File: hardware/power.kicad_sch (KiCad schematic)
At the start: 16 parts, among them J6 USB_C_Receptacle, Q1 DMG2307L, Q2 DMG2307L, Q3 BSD235N, U5 AP9101CK, U6 MIC5504-3.3YM5

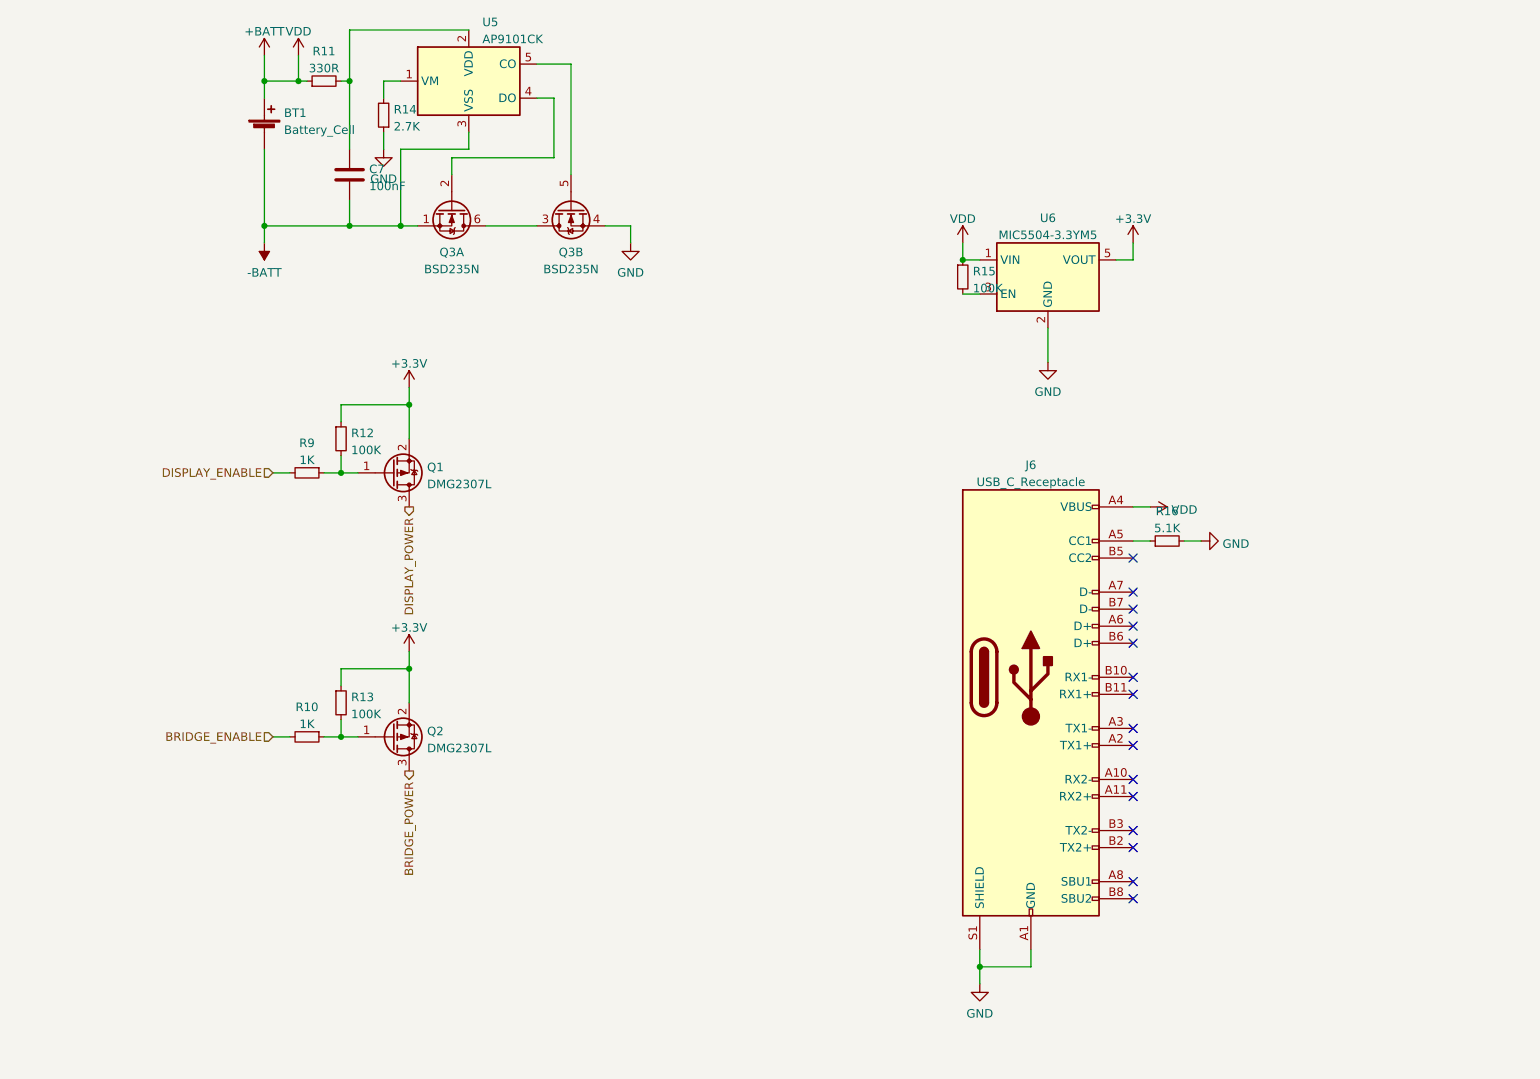
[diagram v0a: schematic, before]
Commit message: Updated schematic according to reference design
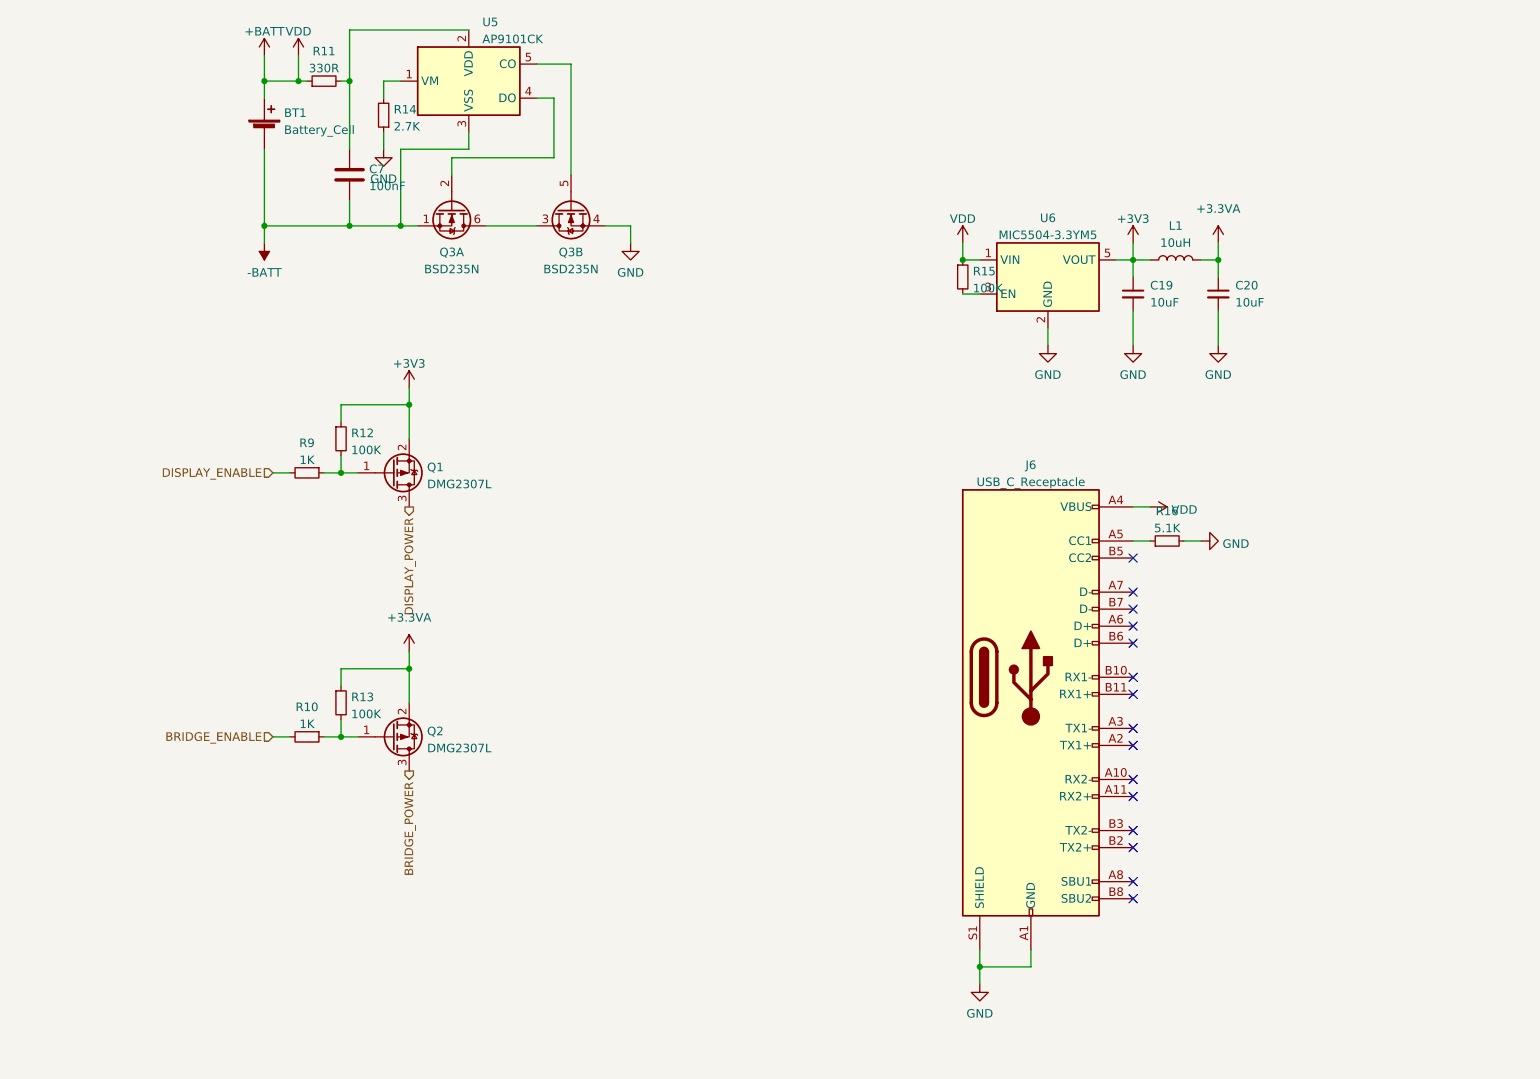
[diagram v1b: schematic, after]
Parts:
- added C19, C20: 10uF, symbol Device:C_Small
- added L1: 10uH, symbol Device:L
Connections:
- net +3V3: now also C19.1, L1.1; no longer Q2.2 (S), R13.1
- net GND: now also C19.2, C20.2
- new net +3.3VA: C20.1, L1.2, Q2.2 (S), R13.1

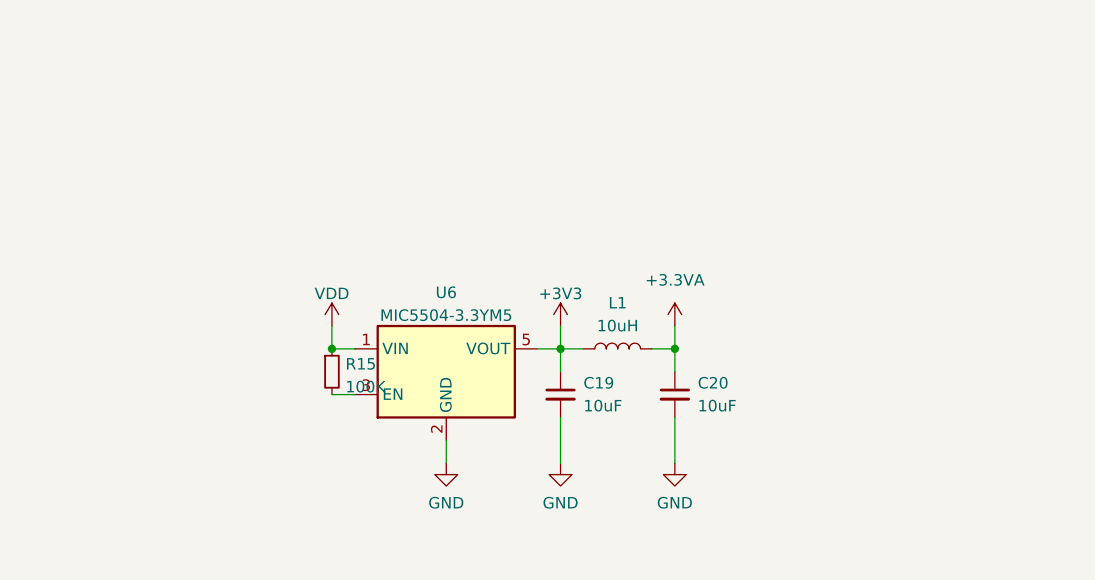
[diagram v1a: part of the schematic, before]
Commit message: Include active filter, ext. ADC, changes to power supply
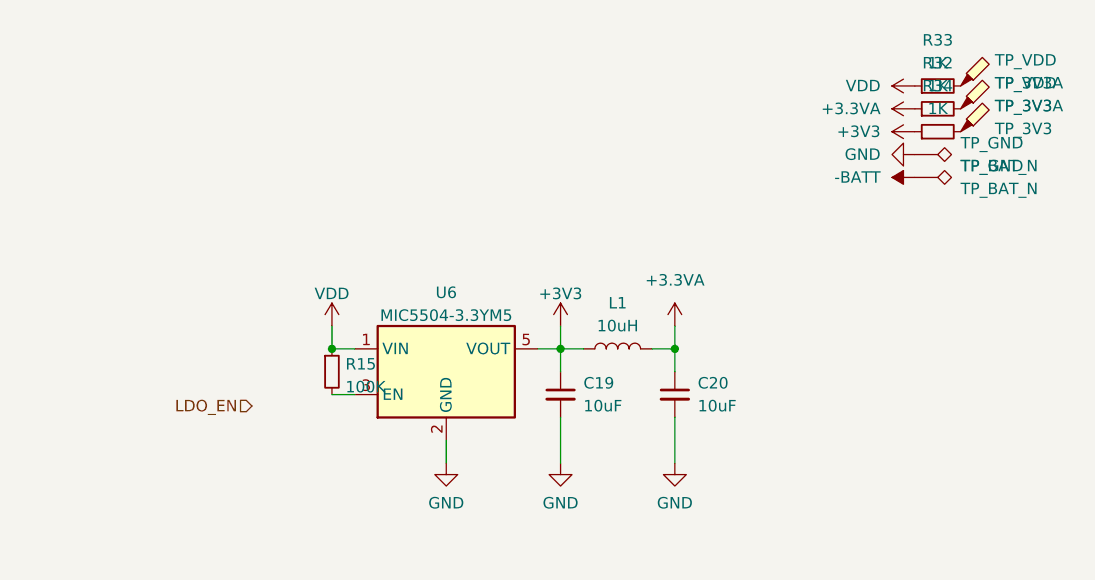
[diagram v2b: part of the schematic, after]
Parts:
- added R32, R33, R34: 1K, Resistor_SMD:R_0603_1608Metric_Pad0.98x0.95mm_HandSolder, symbol Device:R_Small
- added TP_3V3: TP_3V3, symbol Connector:TestPoint_Probe
- added TP_3V3A: TP_3V3A, symbol Connector:TestPoint_Probe
- added TP_BAT_N: TP_BAT_N, symbol Connector:TestPoint_Alt
- added TP_GND: TP_GND, symbol Connector:TestPoint_Alt
- added TP_VDD: TP_VDD, symbol Connector:TestPoint_Probe
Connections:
- net +3.3VA: now also R32.1
- net +3V3: now also R34.1
- net +BATT: now also R33.1
- net -BATT: now also TP_BAT_N.1
- net GND: now also TP_GND.1
- new net: R33.2, TP_VDD.1
- new net: R34.2, TP_3V3.1
- new net: R32.2, TP_3V3A.1

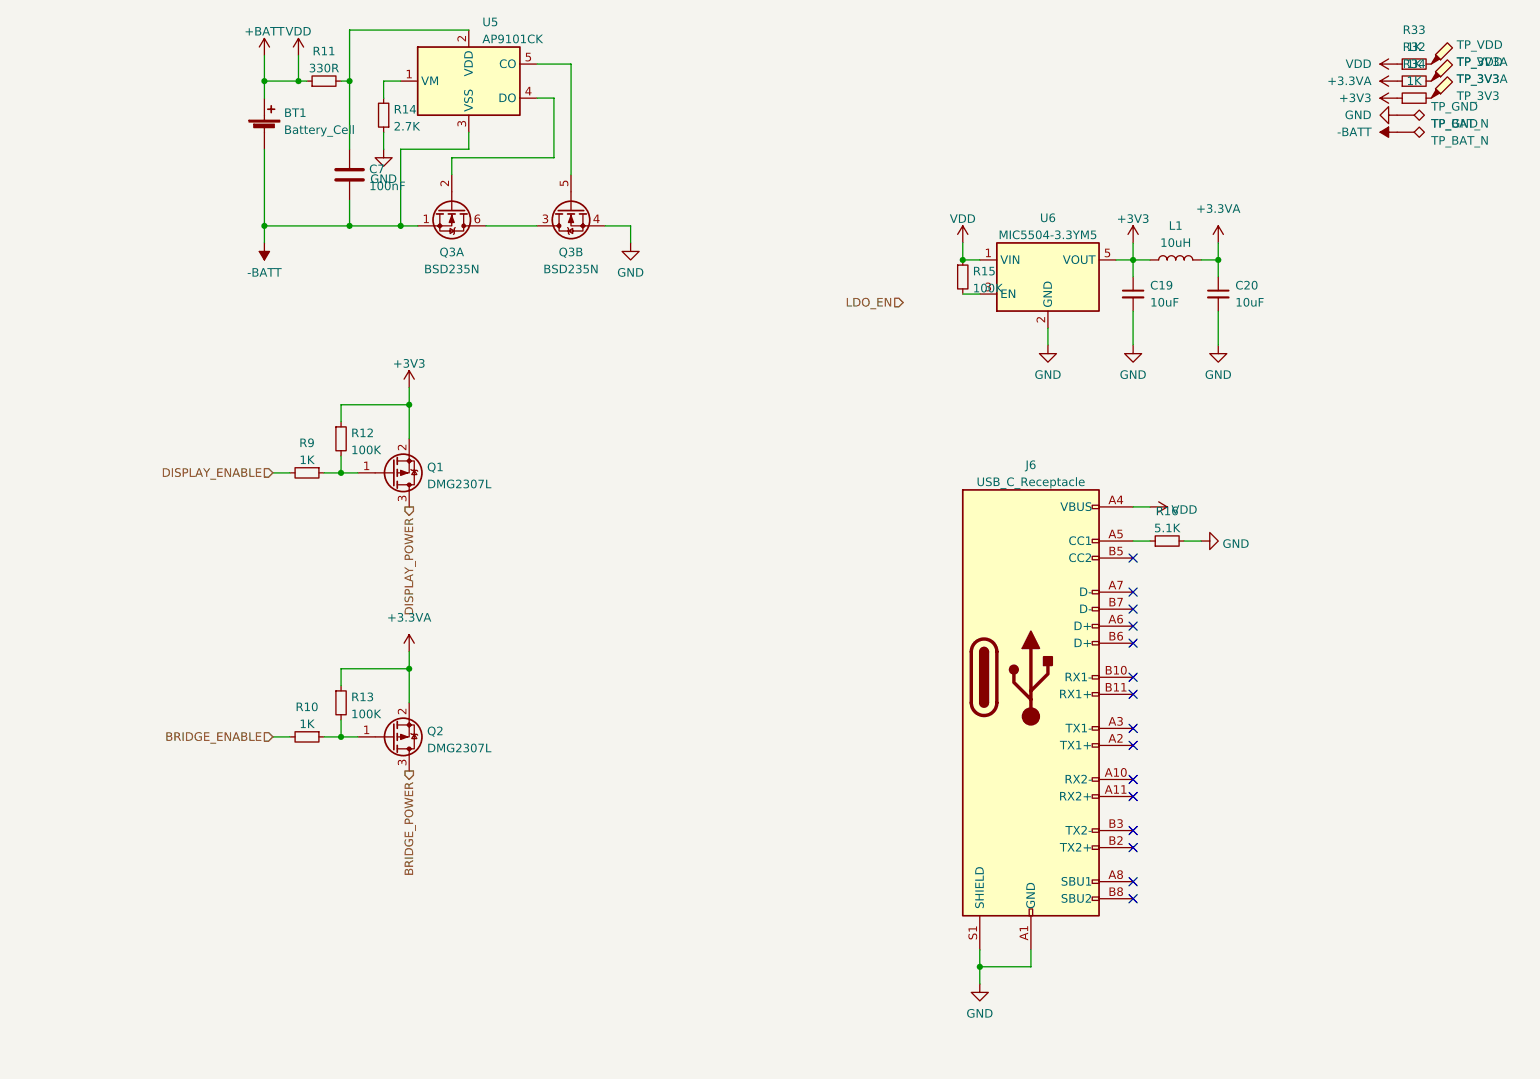
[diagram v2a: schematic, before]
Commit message: Added correct symbol and libraries for ADC
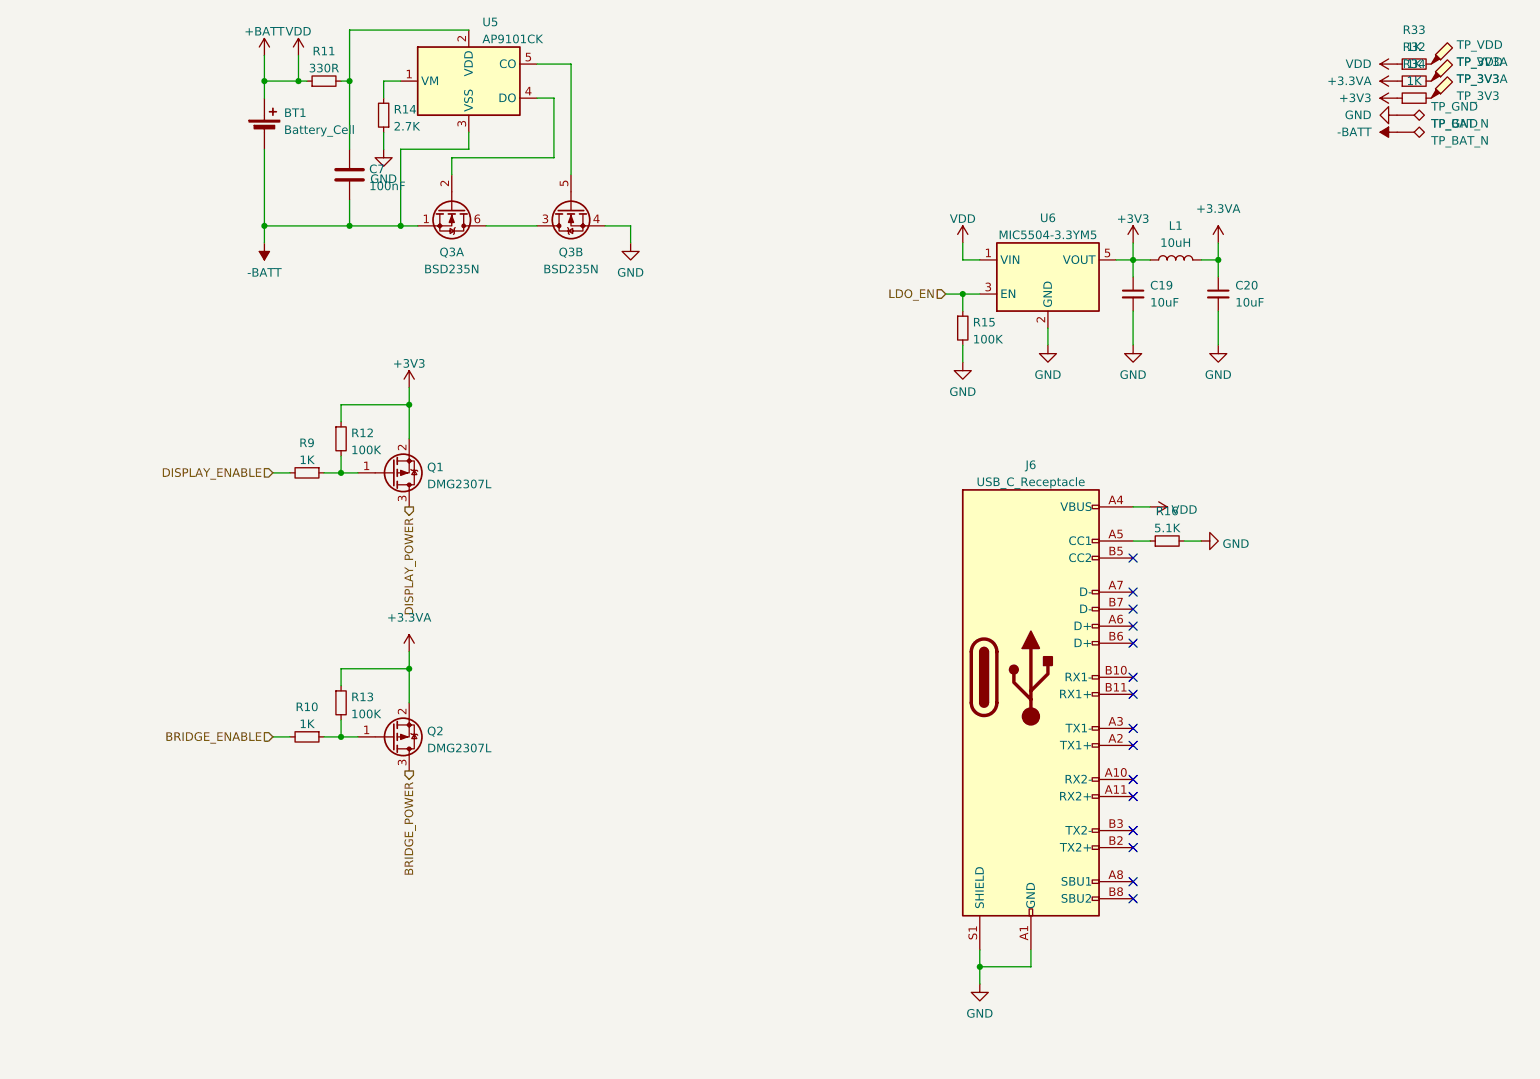
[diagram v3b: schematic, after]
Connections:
- net +BATT: no longer R15.1
- net GND: now also R15.2
- net LDO_EN: now also R15.1, U6.3 (EN)
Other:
- moved on the sheet: R15

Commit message: Regenerated reference designators, changed to rail-to-rail op-amps
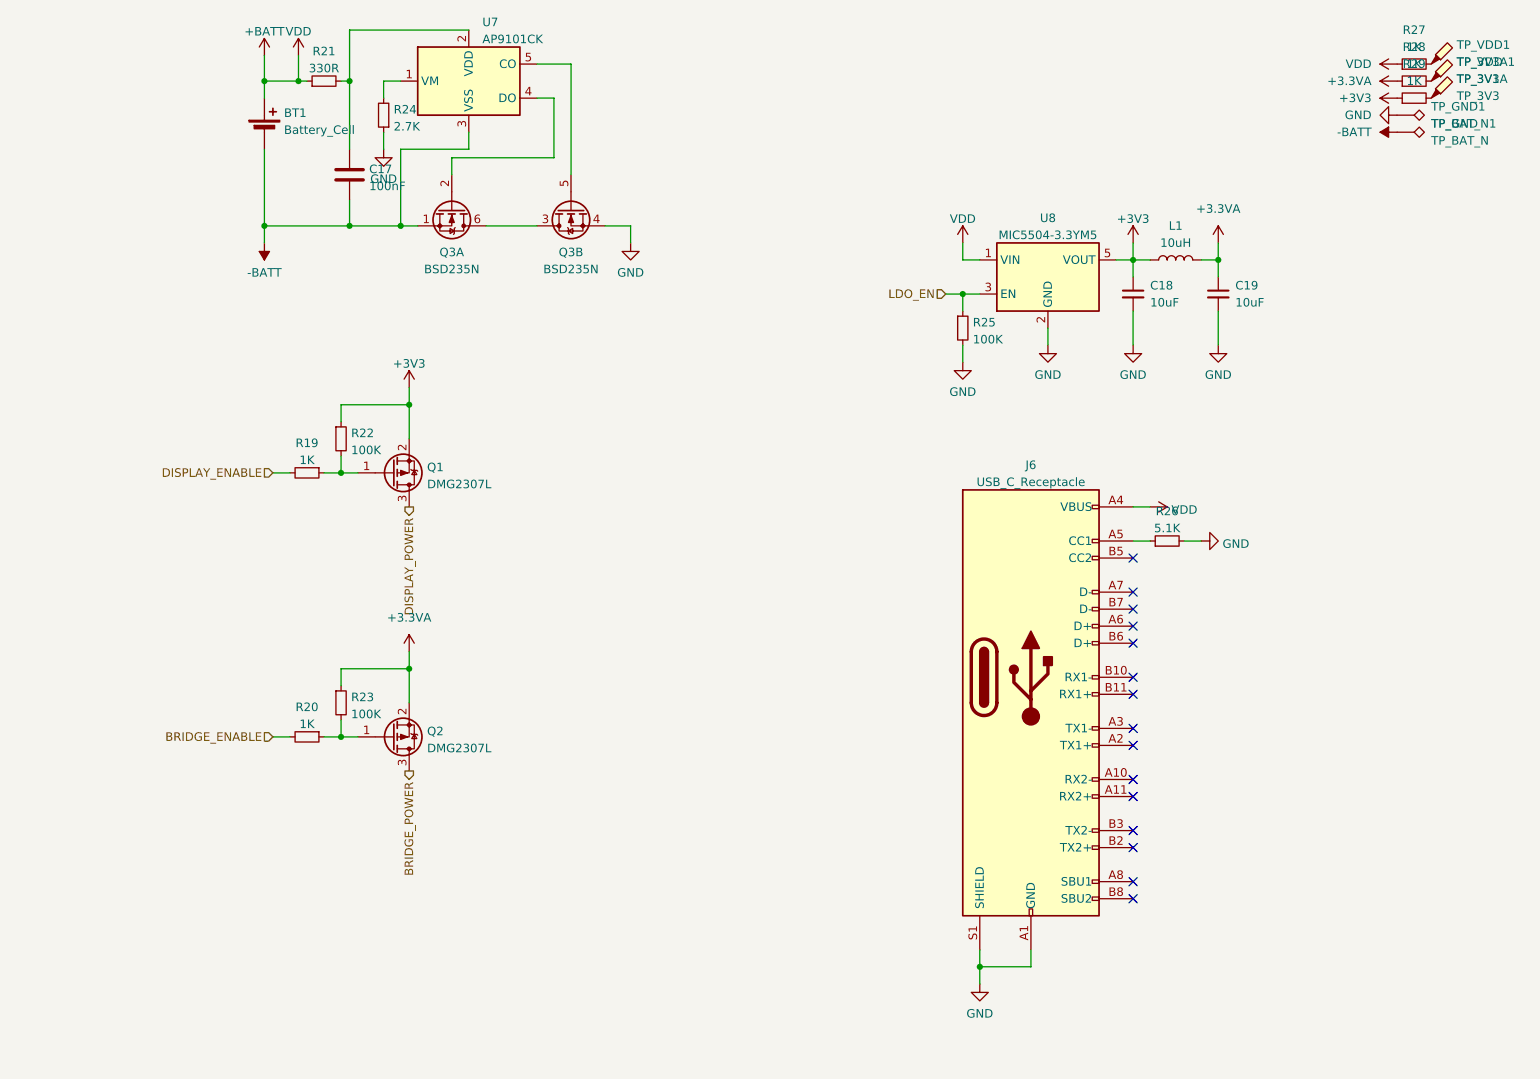
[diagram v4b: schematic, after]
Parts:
- renumbered C7 to C17, C19 to C18, C20 to C19, R9 to R19, R10 to R20, R11 to R21, R12 to R22, R13 to R23, R14 to R24, R15 to R25, R16 to R26, R33 to R27, R32 to R28, R34 to R29, TP_3V3 to TP_3V1, TP_3V3A to TP_3V3A1, TP_BAT_N to TP_BAT_N1, TP_GND to TP_GND1, TP_VDD to TP_VDD1, U5 to U7, U6 to U8

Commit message: Major changes to schematic
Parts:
- removed J6: USB_C_Receptacle, Custom:USB_C_Receptacle_Amphenol_12401610E4-2A, symbol Connector:USB_C_Receptacle
- added J7: 12401610E4#2A, custom:12401610E42A, symbol 12401610E4#2A:12401610E4#2A
- C17: footprint Capacitor_SMD:C_0603_1608Metric_Pad1.08x0.95mm_HandSolder -> Capacitor_SMD:C_0603_1608Metric
- C18, C19: footprint (none) -> Capacitor_SMD:C_1210_3225Metric
- L1: footprint (none) -> Inductor_SMD:L_1210_3225Metric
- R19, R20, R21, R22, R23, R24, R25, R26, R27, R28, R29: footprint Resistor_SMD:R_0603_1608Metric_Pad0.98x0.95mm_HandSolder -> Resistor_SMD:R_0603_1608Metric
- TP_3V1, TP_3V3A1, TP_BAT_N1, TP_GND1, TP_VDD1: footprint (none) -> TestPoint:TestPoint_Pad_D1.5mm
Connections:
- net +BATT: now also J7.A4 (VBUS_1)
- net GND: now also J7.27 (MH1), J7.28 (MH2), J7.29 (MH3), J7.30 (MH4), J7.A1 (GND_1), J7.A12 (GND_2), J7.B1 (GND_3), J7.B12 (GND_4)
- net at R26.1: now also J7.A5 (CC1)
- no-connect marks 15 -> 18
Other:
- moved on the sheet: C18, C19, L1, Q1, Q2, R19, R20, R22, R23, R25, R26, U8
